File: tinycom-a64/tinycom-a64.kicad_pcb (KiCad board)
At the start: 4 copper layers, 41.7 x 40.9 mm, 28 parts, among them P1 CONN_02X10, P2 CONN_02X10, U1 AllWinner-A64(FBGA396), U2 H5TQG63BFR/FBGA96, Y1 Crystal

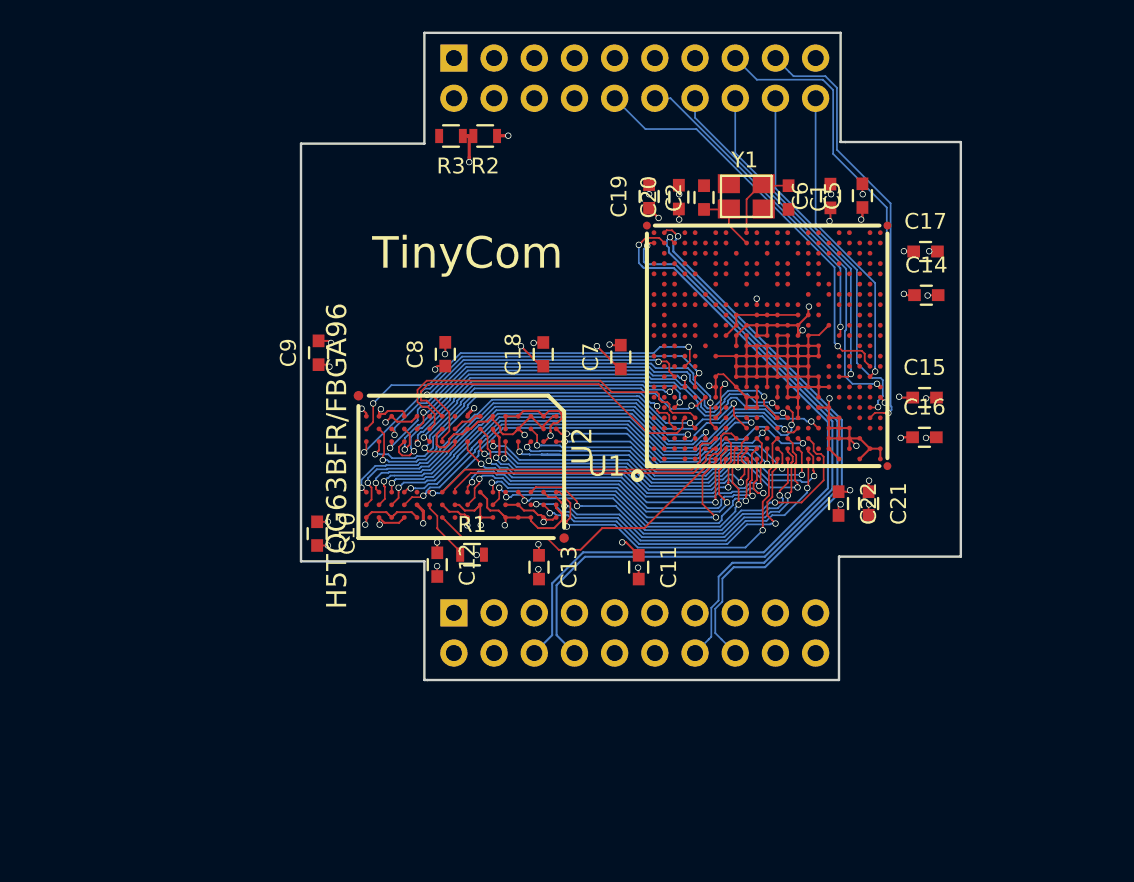
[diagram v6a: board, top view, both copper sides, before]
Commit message: reroute, escape bga
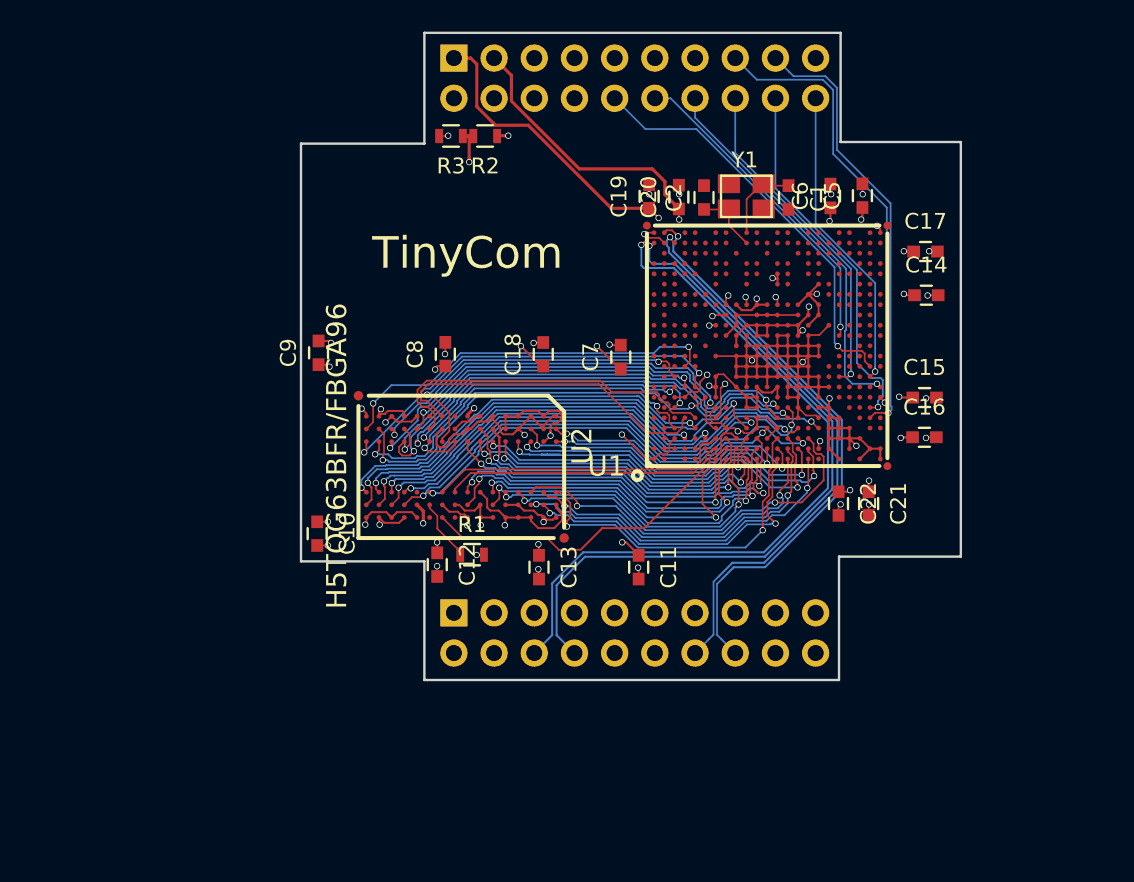
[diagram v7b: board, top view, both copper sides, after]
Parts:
- C1, C2: value C_Small -> 33pF
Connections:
- C14 pad 1: VCC_12 -> VCC_11
- C15 pad 1: VCC_12 -> VCC_11
- C20 pad 1: VCC_12 -> VCC_11
- C22 pad 1: VCC_12 -> VCC_11
- C6 pad 1: VCC_12 -> VCC_11
- P2 pad 3: VCC_12 -> VCC_11
- P2 pad 7: (no net) -> VCC_30
- U1 pad AA1: VCC_12 -> VCC_11
- U1 pad AA3: VCC_12 -> VCC_11
- U1 pad AB2: VCC_12 -> VCC_11
- U1 pad AC1: VCC_12 -> VCC_11
- U1 pad AC2: VCC_12 -> VCC_11
- U1 pad G14: (no net) -> VCC_30
- U1 pad H15: (no net) -> VCC_11
- U1 pad H16: (no net) -> VCC_30
- U1 pad J12: VCC_12 -> VCC_11
- U1 pad J13: VCC_12 -> VCC_11
- U1 pad J16: (no net) -> VCC_33
- U1 pad K14: VCC_12 -> VCC_11
- U1 pad K16: (no net) -> VCC_11
- U1 pad L13: VCC_12 -> VCC_11
- U1 pad L14: VCC_12 -> VCC_11
- U1 pad M13: VCC_12 -> VCC_11
- U1 pad M14: VCC_12 -> VCC_11
- U1 pad M16: (no net) -> VCC_33
- U1 pad N14: VCC_12 -> VCC_11
- U1 pad N16: (no net) -> VCC_30
- U1 pad N18: (no net) -> VCC_33
- U1 pad N19: (no net) -> VCC_33
- U1 pad P14: VCC_12 -> VCC_11
- U1 pad R13: VCC_12 -> VCC_11
- U1 pad R14: VCC_12 -> VCC_11
- U1 pad R16: (no net) -> VCC_33
- U1 pad T14: (no net) -> VCC_33
- U1 pad T15: VCC_12 -> VCC_11
- U1 pad T17: (no net) -> VCC_33
- U1 pad U15: (no net) -> VCC_33
- U1 pad U16: (no net) -> VCC_33
- U1 pad U18: (no net) -> VCC_33
- U1 pad U6: VCC_12 -> VCC_11
- U1 pad V2: VCC_12 -> VCC_11
- U1 pad V3: VCC_12 -> VCC_11
- U1 pad V4: VCC_12 -> VCC_11
- U1 pad V5: VCC_12 -> VCC_11
- U1 pad V6: VCC_12 -> VCC_11
- U1 pad W1: VCC_12 -> VCC_11
- U1 pad W3: VCC_12 -> VCC_11
- U1 pad W4: VCC_12 -> VCC_11
- U1 pad W5: VCC_12 -> VCC_11
- U1 pad Y2: VCC_12 -> VCC_11
- U1 pad Y3: VCC_12 -> VCC_11
- U1 pad Y4: VCC_12 -> VCC_11
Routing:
- net VCC_11: track 0.00 -> 46.8 mm, vias 0 -> 11
- net VCC_33: track 22.2 -> 69.0 mm, vias 6 -> 8
- net VCC_30: track 0.00 -> 30.0 mm, vias 0 -> 3
- net VCC_12: track 28.3 -> 0.00 mm, vias 9 -> 0
- net GND: track 94.2 -> 114.2 mm, vias 25 -> 34
- net VCC_15: track 57.1 -> 60.1 mm
- net UD0_P: track 46.7 -> 46.1 mm
- added copper zone on In2.Cu, net VCC_11
- removed copper zone on In2.Cu, net VCC_12
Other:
- net class Power: trace_width 0.3 -> 0.15

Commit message: a64 update
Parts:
- added P3: CONN_01X03, Pin_Headers:Pin_Header_Angled_1x03, F.Cu at (91.3, 129.9)
- Y1: footprint Crystals:crystal_FA238-TSX3225 -> opendous:Crystal_5x3.2mm
- moved C21 26.0 mm to (105.0, 171.9), turned to 0 degrees
- moved C22 25.0 mm to (105.0, 171.9), turned to 0 degrees
- moved C2 5.90 mm to (114.9, 128.6), turned to 180 degrees
- moved C1 4.14 mm to (111.9, 128.5), turned to 0 degrees
- moved Y1 1.22 mm to (113.4, 130.6), turned to 180 degrees
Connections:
- P1 pad 1: (no net) -> HTX2_P
- P1 pad 10: (no net) -> UD1_N
- P1 pad 11: (no net) -> HTX0_N
- P1 pad 12: (no net) -> Net-(P1-Pad12)
- P1 pad 13: (no net) -> HTXC_P
- P1 pad 14: UD2_N -> Net-(P1-Pad14)
- P1 pad 15: (no net) -> HTXC_N
- P1 pad 16: UD2_P -> Net-(P1-Pad16)
- P1 pad 17: (no net) -> HCEC
- P1 pad 18: (no net) -> HHPD
- P1 pad 19: (no net) -> HSCL
- P1 pad 20: (no net) -> HSDA
- P1 pad 3: (no net) -> HTX2_N
- P1 pad 4: (no net) -> UD0_P
- P1 pad 5: (no net) -> HTX1_P
- P1 pad 7: (no net) -> HTX1_N
- P1 pad 8: UD0_P -> UD1_P
- P1 pad 9: (no net) -> HTX0_P
- P2 pad 1: VCC_33 -> VCC_11_CPU
- P2 pad 11: (no net) -> VCC_30_ANL
- P2 pad 13: (no net) -> Net-(P2-Pad13)
- P2 pad 15: UART0_RX -> UART1_RX
- P2 pad 17: UART0_TX -> UART1_TX
- P2 pad 2: (no net) -> Net-(P2-Pad2)
- P2 pad 3: VCC_11 -> VCC_11_INT
- P2 pad 4: (no net) -> Net-(P2-Pad4)
- P2 pad 5: VCC_15 -> VCC_33
- P2 pad 6: (no net) -> Net-(P2-Pad6)
- P2 pad 7: VCC_30 -> VCC_15
- P2 pad 8: (no net) -> Net-(P2-Pad8)
- P2 pad 9: (no net) -> VCC_13_RTC
- U1 pad A11: (no net) -> Net-(U1-PadA11)
- U1 pad A13: (no net) -> Net-(U1-PadA13)
- U1 pad A14: (no net) -> Net-(U1-PadA14)
- U1 pad A16: (no net) -> Net-(U1-PadA16)
- U1 pad A17: (no net) -> Net-(U1-PadA17)
- U1 pad A19: (no net) -> Net-(U1-PadA19)
- U1 pad A2: (no net) -> SDQ22
- U1 pad A20: (no net) -> Net-(U1-PadA20)
- U1 pad A4: (no net) -> SDQ26
- U1 pad A5: (no net) -> SDQ27
- U1 pad A7: (no net) -> SDQ28
- U1 pad A8: (no net) -> SDQ29
- U1 pad AA1: VCC_11 -> VCC_11_CPU
- U1 pad AA10: (no net) -> Net-(U1-PadAA10)
- U1 pad AA11: (no net) -> Net-(U1-PadAA11)
- U1 pad AA12: (no net) -> Net-(U1-PadAA12)
- U1 pad AA13: (no net) -> Net-(U1-PadAA13)
- U1 pad AA14: (no net) -> Net-(U1-PadAA14)
- U1 pad AA15: (no net) -> Net-(U1-PadAA15)
- U1 pad AA16: (no net) -> Net-(U1-PadAA16)
- U1 pad AA17: (no net) -> Net-(U1-PadAA17)
- U1 pad AA18: (no net) -> Net-(U1-PadAA18)
- U1 pad AA19: (no net) -> Net-(U1-PadAA19)
- U1 pad AA20: (no net) -> Net-(U1-PadAA20)
- U1 pad AA21: (no net) -> Net-(U1-PadAA21)
- U1 pad AA22: (no net) -> Net-(U1-PadAA22)
- U1 pad AA3: VCC_11 -> VCC_11_CPU
- U1 pad AA5: (no net) -> Net-(U1-PadAA5)
- U1 pad AA6: (no net) -> Net-(U1-PadAA6)
- U1 pad AA7: (no net) -> Net-(U1-PadAA7)
- U1 pad AA8: (no net) -> Net-(U1-PadAA8)
- U1 pad AA9: (no net) -> Net-(U1-PadAA9)
- U1 pad AB11: (no net) -> Net-(U1-PadAB11)
- U1 pad AB12: (no net) -> Net-(U1-PadAB12)
- U1 pad AB13: (no net) -> Net-(U1-PadAB13)
- U1 pad AB14: (no net) -> Net-(U1-PadAB14)
- U1 pad AB15: (no net) -> Net-(U1-PadAB15)
- U1 pad AB16: (no net) -> Net-(U1-PadAB16)
- U1 pad AB17: (no net) -> UART1_TX
- U1 pad AB18: (no net) -> Net-(U1-PadAB18)
- U1 pad AB19: (no net) -> Net-(U1-PadAB19)
- U1 pad AB2: VCC_11 -> VCC_11_CPU
- U1 pad AB20: (no net) -> Net-(U1-PadAB20)
- U1 pad AB21: (no net) -> Net-(U1-PadAB21)
- U1 pad AB22: (no net) -> Net-(U1-PadAB22)
- U1 pad AB23: (no net) -> Net-(U1-PadAB23)
- U1 pad AB4: (no net) -> Net-(U1-PadAB4)
- U1 pad AB5: UART0_TX -> UART3_TX
- U1 pad AB7: (no net) -> UART2_RX
- U1 pad AB8: (no net) -> Net-(U1-PadAB8)
- U1 pad AC1: VCC_11 -> VCC_11_CPU
- U1 pad AC10: (no net) -> Net-(U1-PadAC10)
- U1 pad AC11: (no net) -> Net-(U1-PadAC11)
- U1 pad AC13: (no net) -> Net-(U1-PadAC13)
- U1 pad AC14: (no net) -> Net-(U1-PadAC14)
- U1 pad AC16: (no net) -> Net-(U1-PadAC16)
- U1 pad AC17: (no net) -> Net-(U1-PadAC17)
- U1 pad AC19: (no net) -> Net-(U1-PadAC19)
- U1 pad AC2: VCC_11 -> VCC_11_CPU
- U1 pad AC20: (no net) -> Net-(U1-PadAC20)
- U1 pad AC22: (no net) -> Net-(U1-PadAC22)
- U1 pad AC4: (no net) -> Net-(U1-PadAC4)
- U1 pad AC5: (no net) -> Net-(U1-PadAC5)
- U1 pad AC7: UART0_RX -> UART3_RX
- U1 pad B1: (no net) -> SDQ20
- U1 pad B10: (no net) -> Net-(U1-PadB10)
- U1 pad B11: (no net) -> Net-(U1-PadB11)
- U1 pad B12: (no net) -> Net-(U1-PadB12)
- U1 pad B13: (no net) -> Net-(U1-PadB13)
- U1 pad B14: (no net) -> Net-(U1-PadB14)
- U1 pad B15: (no net) -> Net-(U1-PadB15)
- U1 pad B16: (no net) -> Net-(U1-PadB16)
- U1 pad B17: (no net) -> Net-(U1-PadB17)
- U1 pad B18: (no net) -> Net-(U1-PadB18)
- U1 pad B19: (no net) -> Net-(U1-PadB19)
- U1 pad B2: (no net) -> SDQ21
- U1 pad B20: (no net) -> Net-(U1-PadB20)
- U1 pad B21: (no net) -> Net-(U1-PadB21)
- U1 pad B23: UD2_P -> UD1_P
- U1 pad B3: (no net) -> SDQ23
- U1 pad B4: (no net) -> SDQ25
- U1 pad B5: (no net) -> Net-(U1-PadB5)
- U1 pad B6: (no net) -> Net-(U1-PadB6)
- U1 pad B7: (no net) -> Net-(U1-PadB7)
- U1 pad B8: (no net) -> SDQ30
- U1 pad B9: (no net) -> SDQ31
- U1 pad C10: (no net) -> Net-(U1-PadC10)
- U1 pad C11: (no net) -> Net-(U1-PadC11)
- U1 pad C12: (no net) -> Net-(U1-PadC12)
- U1 pad C13: (no net) -> Net-(U1-PadC13)
- U1 pad C14: (no net) -> Net-(U1-PadC14)
- U1 pad C16: (no net) -> Net-(U1-PadC16)
- U1 pad C17: (no net) -> Net-(U1-PadC17)
- U1 pad C18: (no net) -> Net-(U1-PadC18)
- U1 pad C19: (no net) -> Net-(U1-PadC19)
- U1 pad C2: (no net) -> Net-(U1-PadC2)
- U1 pad C20: (no net) -> Net-(U1-PadC20)
- U1 pad C22: UD2_N -> UD1_N
- U1 pad C5: (no net) -> SDQ24
- U1 pad D1: (no net) -> Net-(U1-PadD1)
- U1 pad D11: (no net) -> Net-(U1-PadD11)
- U1 pad D13: (no net) -> Net-(U1-PadD13)
- U1 pad D14: (no net) -> Net-(U1-PadD14)
- U1 pad D16: (no net) -> Net-(U1-PadD16)
- U1 pad D17: (no net) -> Net-(U1-PadD17)
- U1 pad D19: (no net) -> Net-(U1-PadD19)
- U1 pad D2: (no net) -> Net-(U1-PadD2)
- U1 pad D20: (no net) -> Net-(U1-PadD20)
- U1 pad D21: (no net) -> Net-(U1-PadD21)
- U1 pad D22: (no net) -> Net-(U1-PadD22)
- U1 pad D23: (no net) -> HTX2_P
- U1 pad E1: (no net) -> SDQ19
- U1 pad E10: (no net) -> Net-(U1-PadE10)
- U1 pad E11: (no net) -> Net-(U1-PadE11)
- U1 pad E13: (no net) -> Net-(U1-PadE13)
- U1 pad E14: (no net) -> Net-(U1-PadE14)
- U1 pad E16: (no net) -> Net-(U1-PadE16)
- U1 pad E17: (no net) -> Net-(U1-PadE17)
- U1 pad E19: (no net) -> Net-(U1-PadE19)
- U1 pad E2: (no net) -> SDQ18
- U1 pad E20: (no net) -> HSDA
- U1 pad E21: (no net) -> HHPD
- U1 pad E22: (no net) -> HTX2_N
- U1 pad E23: (no net) -> HTX1_P
- U1 pad E3: (no net) -> SDQ16
- U1 pad E7: (no net) -> Net-(U1-PadE7)
- U1 pad F12: (no net) -> Net-(U1-PadF12)
- U1 pad F16: (no net) -> Net-(U1-PadF16)
- U1 pad F17: (no net) -> Net-(U1-PadF17)
- U1 pad F2: (no net) -> SDQ17
- U1 pad F21: (no net) -> HCEC
- U1 pad F22: (no net) -> HTX1_N
- U1 pad G13: (no net) -> Net-(U1-PadG13)
- U1 pad G16: (no net) -> Net-(U1-PadG16)
- U1 pad G18: (no net) -> Net-(U1-PadG18)
- U1 pad G19: (no net) -> Net-(U1-PadG19)
- U1 pad G20: (no net) -> Net-(U1-PadG20)
- U1 pad G21: (no net) -> HSCL
- U1 pad G22: (no net) -> HTX0_P
- U1 pad G23: (no net) -> HTX0_N
- U1 pad H14: (no net) -> Net-(U1-PadH14)
- U1 pad H15: VCC_11 -> VCC_11_CPU
- U1 pad H16: VCC_30 -> VCC_13_RTC
- U1 pad H19: (no net) -> Net-(U1-PadH19)
- U1 pad H20: (no net) -> Net-(U1-PadH20)
- U1 pad H22: (no net) -> HTXC_P
- U1 pad H23: (no net) -> HTXC_N
- U1 pad H5: (no net) -> Net-(U1-PadH5)
- U1 pad H6: (no net) -> Net-(U1-PadH6)
- U1 pad J12: VCC_11 -> VCC_11_INT
- U1 pad J13: VCC_11 -> VCC_11_INT
- U1 pad J21: (no net) -> Net-(U1-PadJ21)
- U1 pad K14: VCC_11 -> VCC_11_INT
- U1 pad K16: VCC_11 -> VCC_11_INT
- U1 pad K18: (no net) -> Net-(U1-PadK18)
- U1 pad K19: (no net) -> Net-(U1-PadK19)
- U1 pad K20: (no net) -> Net-(U1-PadK20)
- U1 pad L13: VCC_11 -> VCC_11_INT
- U1 pad L14: VCC_11 -> VCC_11_INT
- U1 pad L19: (no net) -> Net-(U1-PadL19)
- U1 pad L20: (no net) -> Net-(U1-PadL20)
- U1 pad L22: (no net) -> Net-(U1-PadL22)
- U1 pad L23: (no net) -> Net-(U1-PadL23)
- U1 pad M13: VCC_11 -> VCC_11_INT
- U1 pad M14: VCC_11 -> VCC_11_INT
- U1 pad M21: (no net) -> Net-(U1-PadM21)
- U1 pad M22: (no net) -> Net-(U1-PadM22)
- U1 pad N14: VCC_11 -> VCC_11_INT
- U1 pad N16: VCC_30 -> VCC_33
- U1 pad N20: (no net) -> Net-(U1-PadN20)
- U1 pad N22: (no net) -> Net-(U1-PadN22)
- U1 pad N23: (no net) -> Net-(U1-PadN23)
- U1 pad P14: VCC_11 -> VCC_11_INT
- U1 pad P16: (no net) -> Net-(U1-PadP16)
- U1 pad P18: (no net) -> Net-(U1-PadP18)
- U1 pad P19: (no net) -> Net-(U1-PadP19)
- U1 pad P20: (no net) -> Net-(U1-PadP20)
- U1 pad P22: (no net) -> Net-(U1-PadP22)
- U1 pad P23: (no net) -> Net-(U1-PadP23)
- U1 pad R13: VCC_11 -> VCC_11_INT
- U1 pad R14: VCC_11 -> VCC_11_INT
- U1 pad R21: (no net) -> Net-(U1-PadR21)
- U1 pad R22: (no net) -> Net-(U1-PadR22)
- U1 pad T15: VCC_11 -> VCC_11_INT
- U1 pad T19: (no net) -> Net-(U1-PadT19)
- U1 pad T20: (no net) -> Net-(U1-PadT20)
- U1 pad T21: (no net) -> Net-(U1-PadT21)
- U1 pad T22: (no net) -> Net-(U1-PadT22)
- U1 pad T23: (no net) -> Net-(U1-PadT23)
- U1 pad T4: (no net) -> SA15
- U1 pad T6: (no net) -> Net-(U1-PadT6)
- U1 pad U1: (no net) -> SZQ
- U1 pad U19: (no net) -> Net-(U1-PadU19)
- U1 pad U20: (no net) -> Net-(U1-PadU20)
- U1 pad U21: (no net) -> Net-(U1-PadU21)
- U1 pad U22: (no net) -> Net-(U1-PadU22)
- U1 pad U23: (no net) -> UART1_RX
- U1 pad U6: VCC_11 -> VCC_11_CPU
- U1 pad V10: (no net) -> Net-(U1-PadV10)
- U1 pad V17: (no net) -> Net-(U1-PadV17)
- U1 pad V18: (no net) -> Net-(U1-PadV18)
- U1 pad V2: VCC_11 -> VCC_11_CPU
- U1 pad V21: (no net) -> Net-(U1-PadV21)
- U1 pad V22: (no net) -> Net-(U1-PadV22)
- U1 pad V3: VCC_11 -> VCC_11_CPU
- U1 pad V4: VCC_11 -> VCC_11_CPU
- U1 pad V5: VCC_11 -> VCC_11_CPU
- U1 pad V6: VCC_11 -> VCC_11_CPU
- U1 pad V9: (no net) -> UART2_TX
- U1 pad W1: VCC_11 -> VCC_11_CPU
- U1 pad W10: (no net) -> Net-(U1-PadW10)
- U1 pad W11: (no net) -> Net-(U1-PadW11)
- U1 pad W16: (no net) -> Net-(U1-PadW16)
- U1 pad W17: (no net) -> Net-(U1-PadW17)
- U1 pad W19: (no net) -> Net-(U1-PadW19)
- U1 pad W20: (no net) -> Net-(U1-PadW20)
- U1 pad W21: (no net) -> Net-(U1-PadW21)
- U1 pad W22: (no net) -> Net-(U1-PadW22)
- U1 pad W23: (no net) -> Net-(U1-PadW23)
- U1 pad W3: VCC_11 -> VCC_11_CPU
- U1 pad W4: VCC_11 -> VCC_11_CPU
- U1 pad W5: VCC_11 -> VCC_11_CPU
- U1 pad W7: (no net) -> Net-(U1-PadW7)
- U1 pad W8: (no net) -> Net-(U1-PadW8)
- U1 pad Y10: (no net) -> Net-(U1-PadY10)
- U1 pad Y11: (no net) -> Net-(U1-PadY11)
- U1 pad Y13: (no net) -> Net-(U1-PadY13)
- U1 pad Y14: (no net) -> Net-(U1-PadY14)
- U1 pad Y16: (no net) -> Net-(U1-PadY16)
- U1 pad Y17: (no net) -> Net-(U1-PadY17)
- U1 pad Y19: (no net) -> Net-(U1-PadY19)
- U1 pad Y2: VCC_11 -> VCC_11_CPU
- U1 pad Y21: (no net) -> Net-(U1-PadY21)
- U1 pad Y22: (no net) -> Net-(U1-PadY22)
- U1 pad Y23: (no net) -> Net-(U1-PadY23)
- U1 pad Y3: VCC_11 -> VCC_11_CPU
- U1 pad Y4: VCC_11 -> VCC_11_CPU
- U1 pad Y6: (no net) -> Net-(U1-PadY6)
- U1 pad Y7: (no net) -> Net-(U1-PadY7)
- U1 pad Y8: (no net) -> Net-(U1-PadY8)
- U2 pad J1: (no net) -> Net-(U2-PadJ1)
- U2 pad J9: (no net) -> Net-(U2-PadJ9)
- U2 pad L1: (no net) -> Net-(U2-PadL1)
- U2 pad L9: (no net) -> Net-(U2-PadL9)
- U2 pad M7: (no net) -> Net-(U2-PadM7)
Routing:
- net UART3_RX: track 0.00 -> 51.1 mm, vias 0 -> 3
- net UART3_TX: track 0.00 -> 50.7 mm, vias 0 -> 3
- net HTX2_P: track 0.00 -> 49.7 mm, vias 0 -> 1
- net HTX2_N: track 0.00 -> 48.0 mm, vias 0 -> 1
- net UD1_P: track 0.00 -> 45.7 mm, vias 0 -> 2
- net HTX1_P: track 0.00 -> 44.8 mm, vias 0 -> 1
- net UD1_N: track 0.00 -> 44.8 mm, vias 0 -> 2
- net HTX1_N: track 0.00 -> 43.1 mm, vias 0 -> 1
- net HTX0_P: track 0.00 -> 40.8 mm, vias 0 -> 1
- net HTX0_N: track 0.00 -> 37.6 mm, vias 0 -> 1
- net UD2_P: track 36.9 -> 0.00 mm, vias 1 -> 0
- net UD2_N: track 36.2 -> 0.00 mm, vias 1 -> 0
- net VCC_11: track 46.8 -> 10.6 mm, vias 11 -> 4
- net HTXC_P: track 0.00 -> 36.0 mm, vias 0 -> 1
- net HHPD: track 0.00 -> 34.6 mm, vias 0 -> 1
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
